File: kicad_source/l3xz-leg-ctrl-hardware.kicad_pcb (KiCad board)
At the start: 2 copper layers, 178 x 29 mm, 59 parts, among them CN1 ARDUINO_NANO_33, CN2 SM04B-SRSS-TB, CN3 SM04B-SRSS-TB, CN4 GH_SM04B-GHS-TB, CN5 GH_SM04B-GHS-TB, CN6 691322310002, CN7 CONN_02X03, CN8 WAGO 733-362, U1 AS5048A, U2 AS5048A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

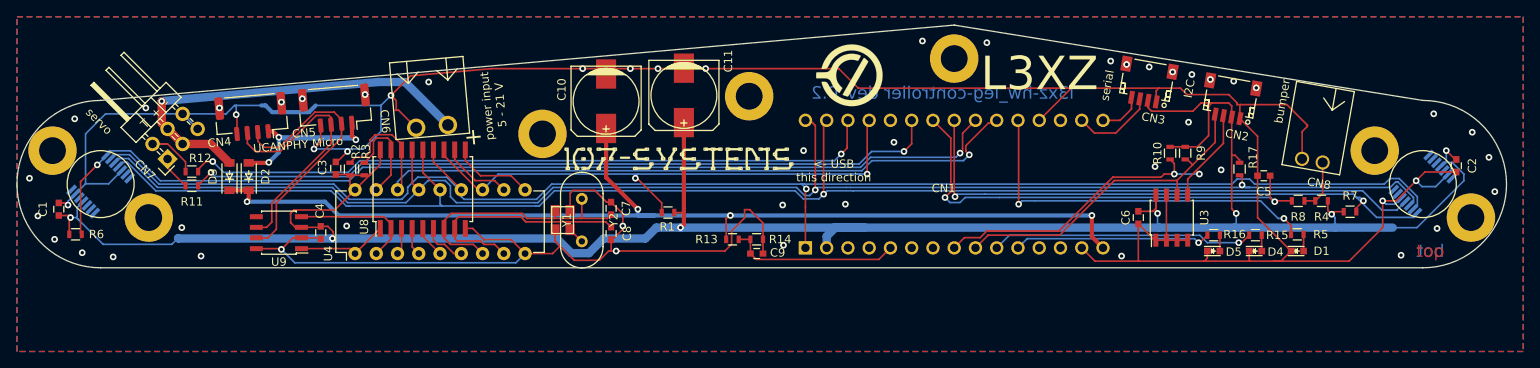
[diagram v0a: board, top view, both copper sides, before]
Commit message: updated footprint library
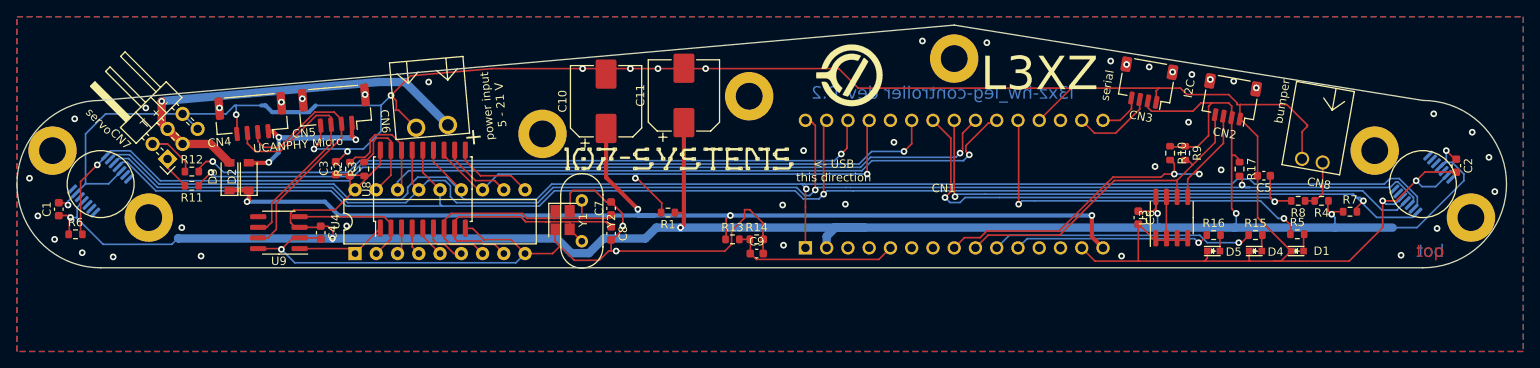
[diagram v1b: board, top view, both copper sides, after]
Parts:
- C1, C2, C3, C4, C5, C6, C7, C8, C9: footprint capacitors:C_0603 -> Capacitor_SMD:C_0603_1608Metric
- C10, C11: footprint capacitors:c_elec_8x10 -> Capacitor_SMD:CP_Elec_8x10
- CN2, CN3: footprint connectors_JST_SH:Connectors_JST_SM04B-SRSS-TB -> Connector_JST:JST_SH_SM04B-SRSS-TB_1x04-1MP_P1.00mm_Horizontal
- CN7: footprint pin_headers:Pin_Header_Angled_2x03 -> Connector_PinHeader_2.54mm:PinHeader_2x03_P2.54mm_Horizontal
- D2, D3: footprint diodes:SOD-123 -> Diode_SMD:D_SOD-123
- R1, R10, R11, R12, R13, R14, R15, R16, R17, R2, R3, R4, R5, R6, R7, R8, R9: footprint resistors:R_0603 -> Resistor_SMD:R_0603_1608Metric
- U1, U2: footprint SSOP:TSSOP-14_4.4x5mm_Pitch0.65mm -> Package_SO:TSSOP-14_4.4x5mm_P0.65mm
- U3, U9: footprint SOIC:SOIC-8_3.9x4.9mm_Pitch1.27mm -> Package_SO:SOIC-8_3.9x4.9mm_P1.27mm
- U4: footprint DIP:DIP-18_W7.62mm -> Package_DIP:DIP-18_W7.62mm
- U8: footprint SOIC:SOIC-18_7.5x11.6mm_Pitch1.27mm -> Package_SO:SOIC-18W_7.5x11.6mm_P1.27mm
- Y1: footprint crystals:Crystal_SMD_3.2x2.5mm_4Pad -> Crystal:Crystal_SMD_3225-4Pin_3.2x2.5mm
- Y2: footprint crystals:HC-49V -> Crystal:Crystal_HC49-U_Vertical
- moved Y2 2.35 mm to (107.5, 92.0)
- turned C10 to 90 degrees
- turned C11 to 90 degrees
- turned Y1 to -90 degrees
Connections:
- net +3V3 renamed +3.3V
- CN1 pad 12: (no net) -> unconnected-(CN1-Pad12)
- CN1 pad 13: (no net) -> unconnected-(CN1-Pad13)
- CN1 pad 18: (no net) -> unconnected-(CN1-Pad18)
- CN1 pad 26: (no net) -> unconnected-(CN1-Pad26)
- CN1 pad 3: (no net) -> unconnected-(CN1-Pad3)
- CN1 pad 4: (no net) -> unconnected-(CN1-Pad4)
- CN1 pad 6: (no net) -> unconnected-(CN1-Pad6)
- CN1 pad 7: (no net) -> unconnected-(CN1-Pad7)
- MECH1 pad 1: (no net) -> unconnected-(MECH1-Pad1)
- MECH2 pad 1: (no net) -> unconnected-(MECH2-Pad1)
- MECH3 pad 1: (no net) -> unconnected-(MECH3-Pad1)
- MECH4 pad 1: (no net) -> unconnected-(MECH4-Pad1)
- MECH5 pad 1: (no net) -> unconnected-(MECH5-Pad1)
- MECH6 pad 1: (no net) -> unconnected-(MECH6-Pad1)
- MECH7 pad 1: (no net) -> unconnected-(MECH7-Pad1)
- U1 pad 10: (no net) -> unconnected-(U1-Pad10)
- U1 pad 12: (no net) -> unconnected-(U1-Pad12)
- U1 pad 14: (no net) -> unconnected-(U1-Pad14)
- U1 pad 6: (no net) -> unconnected-(U1-Pad6)
- U1 pad 7: (no net) -> unconnected-(U1-Pad7)
- U1 pad 8: (no net) -> unconnected-(U1-Pad8)
- U1 pad 9: (no net) -> unconnected-(U1-Pad9)
- U2 pad 10: (no net) -> unconnected-(U2-Pad10)
- U2 pad 12: (no net) -> unconnected-(U2-Pad12)
- U2 pad 14: (no net) -> unconnected-(U2-Pad14)
- U2 pad 6: (no net) -> unconnected-(U2-Pad6)
- U2 pad 7: (no net) -> unconnected-(U2-Pad7)
- U2 pad 8: (no net) -> unconnected-(U2-Pad8)
- U2 pad 9: (no net) -> unconnected-(U2-Pad9)
- U9 pad 5: (no net) -> unconnected-(U9-Pad5)
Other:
- net class Default removed

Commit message: connected mounting pads of connectors
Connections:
- CN2 pad MP: (no net) -> /MP1
- CN3 pad MP: (no net) -> /MP1
- CN4 pad MP: (no net) -> /MCP2515/MP2
- CN5 pad MP: (no net) -> /MCP2515/MP2
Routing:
- net /MCP2515/MP2: track 0.00 -> 17.5 mm, vias 0 -> 4
- net /MP1: track 0.00 -> 15.8 mm, vias 0 -> 4
- net GND: track 411.5 -> 409.8 mm
- net (no net): vias 8 -> 0

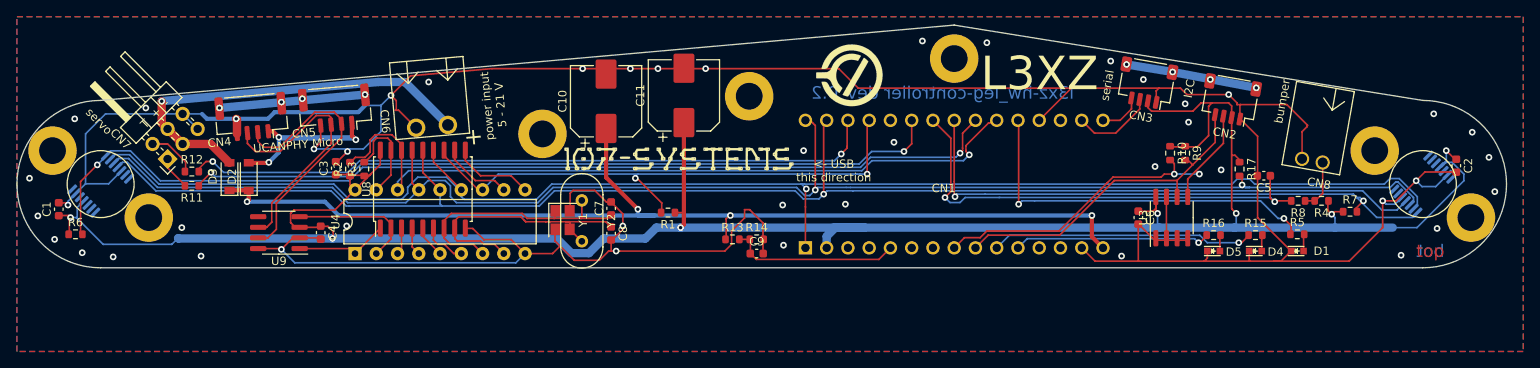
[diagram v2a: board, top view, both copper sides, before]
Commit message: fixed drc errors
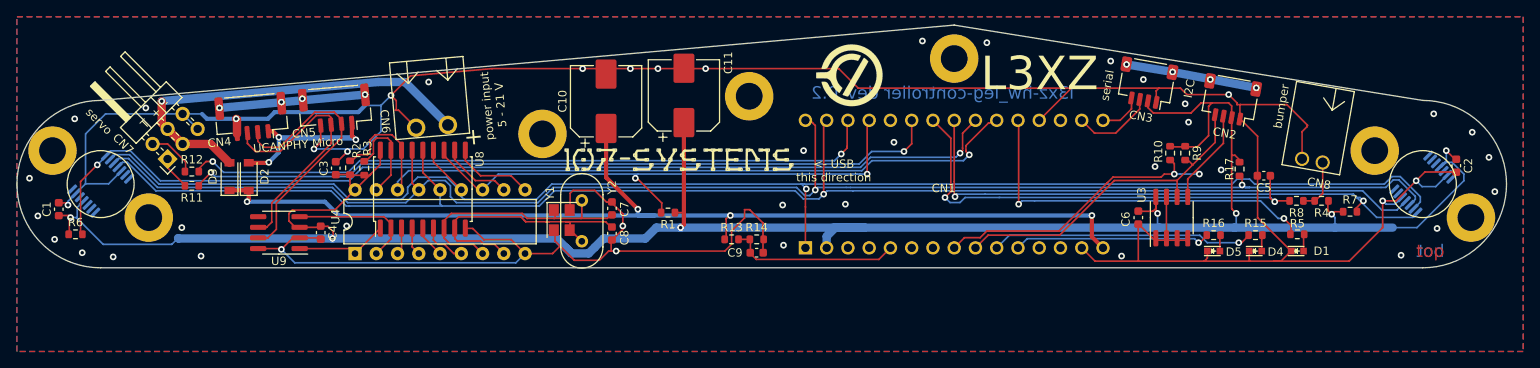
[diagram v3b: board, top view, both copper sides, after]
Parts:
- Y1: footprint Crystal:Crystal_SMD_3225-4Pin_3.2x2.5mm -> Crystal:Crystal_SMD_SeikoEpson_FA238V-4Pin_3.2x2.5mm
- moved R8 0.20 mm to (192.9, 92.0)
- moved R2 0.15 mm to (79.8, 88.0)
- moved R3 0.10 mm to (81.5, 88.1)
- moved Y1 0.10 mm to (105.1, 94.3)
- moved C7 0.10 mm to (111.1, 92.9)
- moved C8 0.10 mm to (111.1, 95.9)
- moved C9 0.10 mm to (128.4, 98.2)
- moved L1 0.10 mm to (119.1, 87.1)
- moved R13 0.10 mm to (125.4, 96.6)
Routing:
- net /SERVO2_R: track 7.63 -> 5.98 mm
- net +3.3V: track 286.3 -> 287.8 mm
- net /MCP2515/CANVCC: track 31.5 -> 30.6 mm
- net SCK: track 179.9 -> 180.5 mm

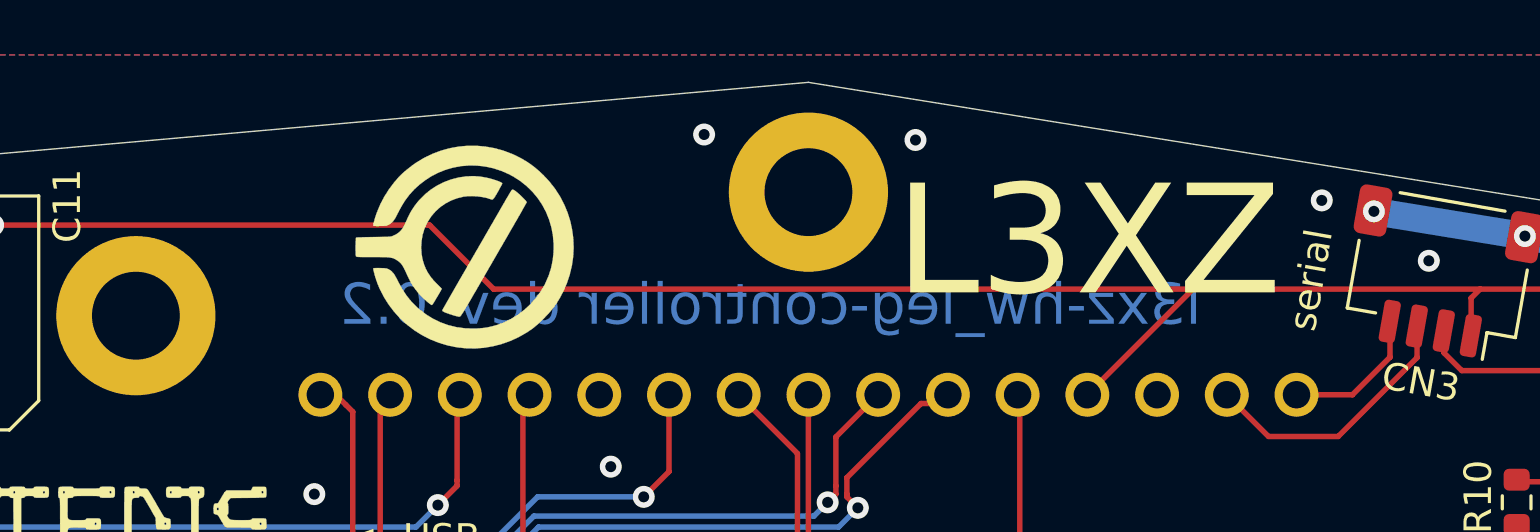
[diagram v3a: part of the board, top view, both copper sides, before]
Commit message: added labels, updated pdf schematic and images
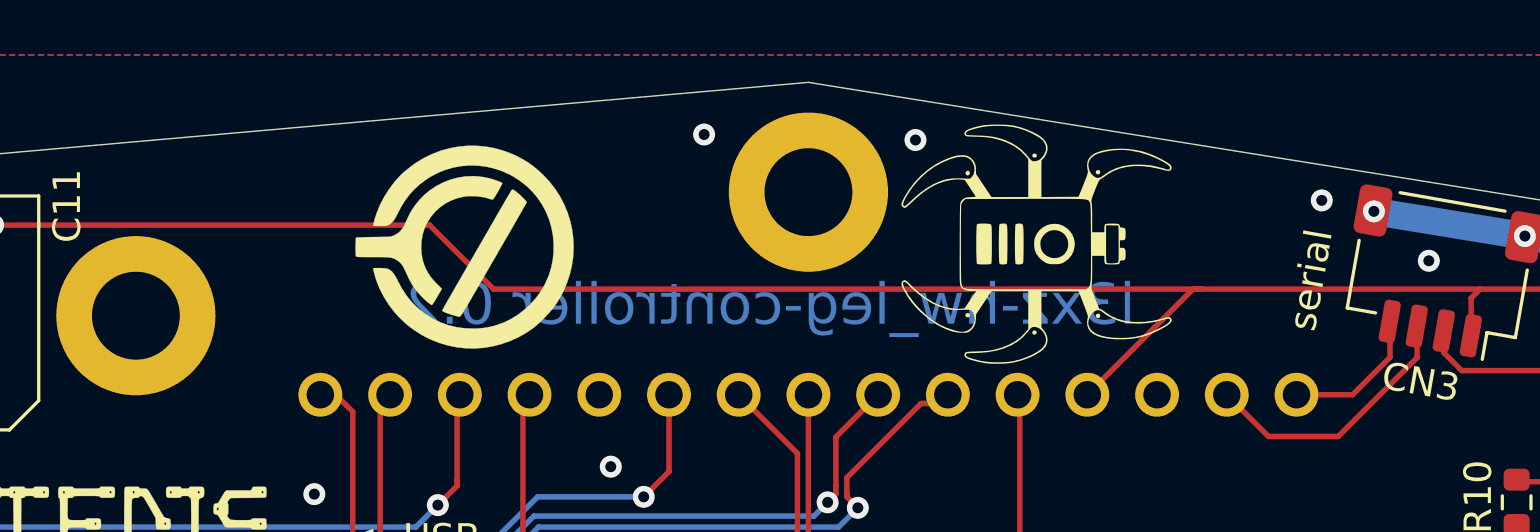
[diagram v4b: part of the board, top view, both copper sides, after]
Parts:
- added L4: Label, generationmake:l3xz_silk, B.Cu at (124.0, 86.8)
- added L5: Label, generationmake:l3xz_small_silk, F.Cu at (160.3, 76.9)
- moved L2 25.7 mm to (171.5, 92.7)
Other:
- board text added: "l3xz-hw_leg-controller 0.2"
- board text removed: "L3XZ"
- board text removed: "l3xz-hw_leg-controller dev_0.2"
